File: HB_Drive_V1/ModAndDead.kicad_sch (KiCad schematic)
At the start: 24 parts, among them J501 Conn_01x02, J502 Conn_01x02, U501 74LS08, U502 74AUC2G02, U503 74LS365, U504 LM311

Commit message: updates board to highest working copy
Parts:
- removed C501, C502, C505, C506, C507, C508: 100nF 100V, Capacitor_SMD:C_0603_1608Metric, symbol Device:C
- removed C503, C504: 470pF 50V, Capacitor_SMD:C_0603_1608Metric, symbol Device:C
- removed J501, J502: Conn_01x02, Jumper:SolderJumper-2_P1.3mm_Open_TrianglePad1.0x1.5mm, symbol Connector_Generic:Conn_01x02
- removed R501, R502: PV36W502C01B00, POT_PV36W_BRN, symbol POT_PV36W_BRN:PV36W502C01B00
- removed R503, R504: 500Ω, Resistor_SMD:R_0603_1608Metric_Pad0.98x0.95mm_HandSolder, symbol Device:R_Small_US
- removed R505, R506: 100KΩ, Resistor_SMD:R_0603_1608Metric_Pad0.98x0.95mm_HandSolder, symbol Device:R_Small_US
- removed R507, R508, R509: 1KΩ, Resistor_SMD:R_0603_1608Metric_Pad0.98x0.95mm_HandSolder, symbol Device:R_Small_US
- removed TP501: TestPoint, TestPoint:TestPoint_Loop_D2.60mm_Drill1.6mm_Beaded, symbol Connector:TestPoint
- removed U501: 74LS08, symbol 74xx:74LS08
- removed U502: 74AUC2G02, symbol 74xGxx:74AUC2G02
- removed U503: 74LS365, symbol 74xx:74LS365
- removed U504: LM311, symbol Comparator:LM311
- added C401, C402, C403, C404, C405, C408: 100nF 100V, Capacitor_SMD:C_0603_1608Metric, symbol Device:C
- added C406, C407: 470pF 50V, Capacitor_SMD:C_0603_1608Metric, symbol Device:C
- added J401, J402: Conn_01x02, Jumper:SolderJumper-2_P1.3mm_Open_TrianglePad1.0x1.5mm, symbol Connector_Generic:Conn_01x02
- added R401, R402, R403: 1KΩ, Resistor_SMD:R_0603_1608Metric_Pad0.98x0.95mm_HandSolder, symbol Device:R_Small_US
- added R404, R405: PV36W502C01B00, POT_PV36W_BRN, symbol POT_PV36W_BRN:PV36W502C01B00
- added R406, R407: 500Ω, Resistor_SMD:R_0603_1608Metric_Pad0.98x0.95mm_HandSolder, symbol Device:R_Small_US
- added R408, R409: 100KΩ, Resistor_SMD:R_0603_1608Metric_Pad0.98x0.95mm_HandSolder, symbol Device:R_Small_US
- added TP401: TestPoint, TestPoint:TestPoint_Loop_D2.60mm_Drill1.6mm_Beaded, symbol Connector:TestPoint
- added U401: LM311, Package_SO:SOIC-8_3.9x4.9mm_P1.27mm, symbol Comparator:LM311
- added U402: 74LS08, Package_SO:SOIC-14_3.9x8.7mm_P1.27mm, symbol 74xx:74LS08
- added U403: 74AUC2G02, Package_SO:VSSOP-8_2.3x2mm_P0.5mm, symbol 74xGxx:74AUC2G02
- added U404: 74LS365, Package_SO:SOIC-16_3.9x9.9mm_P1.27mm, symbol 74xx:74LS365
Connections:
- net +15V: now also C401.1, U401.8 (V+)
- net +5V: now also C403.2, C404.2, C405.2, C408.2, R403.2, U402.7 (GND), U403.4 (GND), U404.16 (VCC)
- net -15V: now also C402.1, U401.4 (V-)
- net Carrier: now also R402.1
- net D_Cmd: now also R401.1
- net GND: now also C401.2, C402.2, C403.1, C404.1, C405.1, C406.2, C407.2, C408.1, R408.2, R409.2, U401.1 (GND), U402.14 (VCC), U403.8 (VCC), U404.1 (E1), U404.12 (I5), U404.14 (I6), U404.15 (E2), U404.4 (I2), U404.6 (I3), U404.8 (GND)
- net G_Lower_Cmd: now also U402.6
- net G_Upper_Cmd: now also U402.3
- net HS_Buf_In: now also C406.1, J401.2 (Pin_2), R406.2, R408.1, U404.2 (I1)
- net HS_Buf_Out: now also J401.1 (Pin_1), U402.2, U404.3 (O1)
- net H_Cmd: now also R403.1, R404.1, R404.2, TP401.1, U401.7, U402.1, U403.1, U403.2
- net LS_Buf_In: now also C407.1, J402.2 (Pin_2), R407.2, R409.1, U404.10 (I4)
- net LS_Buf_Out: now also J402.1 (Pin_1), U402.5, U404.9 (O4)
- new net: R405.3, R407.1
- new net: R401.2, U401.2 (+)
- new net: R404.3, R406.1
- new net: R402.2, U401.3 (-)
- new net: R405.1, R405.2, U402.4, U403.7

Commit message: updates board to REV 1 Ordered version
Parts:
- added unit 2 of U403
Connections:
- net GND: now also U403.5, U403.6
- no-connect marks 6 -> 7
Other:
- note added: "unused NOR 403B on 74AUC2G02 Dual Package"
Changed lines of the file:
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@@
 	)
 	(rectangle
-		(start 171.45 74.93)
+		(start 171.45 58.42)
 		(end 331.47 139.7)
 		(stroke
@@
 	)
 	(rectangle
+		(start 201.93 64.77)
+		(end 252.73 68.58)
+		(stroke
+			(width 0)
+			(type default)
+		)
+		(fill
+			(type none)
+		)
+	)
+	(rectangle
 		(start 238.76 147.32)
 		(end 300.99 208.28)
@@
 		)
 	)
+	(text "unused NOR 403B on 74AUC2G02 Dual Package"
+		(exclude_from_sim no)
+		(at 227.33 66.802 0)
+		(effects
+			(font
+				(size 1.27 1.27)
+			)
+		)
+	)
 	(text "DUTY COMMAND TO CARRIER WAVE COMPARATOR"
 		(exclude_from_sim no)
@@
 	)
 	(junction
+		(at 180.34 78.74)
+		(diameter 0)
+		(color 0 0 0 0)
+	)
+	(junction
 		(at 140.97 97.79)
 		(diameter 0)
@@
 	)
 	(no_connect
+		(at 208.28 76.2)
+	)
+	(no_connect
 		(at 280.67 180.34)
 	)
@@
 	(wire
 		(pts
+			(xy 180.34 73.66) (xy 180.34 78.74)
+		)
+		(stroke
+			(width 0)
+			(type default)
+		)
+	)
+	(wire
+		(pts
 			(xy 252.73 195.58) (xy 267.97 195.58)
 		)
@@
 	(wire
 		(pts
+			(xy 180.34 78.74) (xy 180.34 81.28)
+		)
+		(stroke
+			(width 0)
+			(type default)
+		)
+	)
+	(wire
+		(pts
 			(xy 107.95 113.03) (xy 107.95 107.95)
 		)
@@
 	)
 	(symbol
+		(lib_id "74xGxx:74AUC2G02")
+		(at 195.58 76.2 0)
+		(unit 2)
+		(body_style 1)
+		(exclude_from_sim no)
+		(in_bom yes)
+		(on_board yes)
+		(in_pos_files yes)
+		(dnp no)
+		(fields_autoplaced yes)
+		(property "Reference" "U403"
+			(at 194.31 66.04 0)
+			(show_name no)
+			(do_not_autoplace no)
+			(effects
+				(font
+					(size 1.27 1.27)
+				)
+			)
+		)
+		(property "Value" "74AUC2G02"
+			(at 194.31 68.58 0)
+			(show_name no)
+			(do_not_autoplace no)
+			(effects
+				(font
+					(size 1.27 1.27)
+				)
+			)
+		)
+		(property "Footprint" "Package_SO:VSSOP-8_2.3x2mm_P0.5mm"
+			(at 195.58 76.2 0)
+			(hide yes)
+			(show_name no)
+			(do_not_autoplace no)
+			(effects
+				(font
+					(size 1.27 1.27)
+				)
+			)
+		)
+		(property "Datasheet" "http://www.ti.com/lit/sg/scyt129e/scyt129e.pdf"
+			(at 195.58 76.2 0)
+			(hide yes)
+			(show_name no)
+			(do_not_autoplace no)
+			(effects
+				(font
+					(size 1.27 1.27)
+				)
+			)
+		)
+		(property "Description" "Dual NOR Gate, Low-Voltage CMOS"
+			(at 195.58 76.2 0)
+			(hide yes)
+			(show_name no)
+			(do_not_autoplace no)
+			(effects
+				(font
+					(size 1.27 1.27)
+				)
+			)
+		)
+		(pin "8"
+		)
+		(pin "3"
+		)
+		(pin "4"
+		)
+		(pin "6"
+		)
+		(pin "2"
+		)
+		(pin "5"
+		)
+		(pin "7"
+		)
+		(pin "1"
+		)
+		(instances
+			(project "HB_Drive_V1"
+				(path "/a9b54c89-4c8e-4c90-8a0d-ec2009e369b7/28e2d9d3-ebce-4623-8c7e-52f93025d826/97cfd595-263d-4fe9-9bac-f56dcdbd61fb"
+					(reference "U403")
+					(unit 2)
+				)
+			)
+		)
+	)
+	(symbol
 		(lib_id "Device:C")
 		(at 259.08 125.73 0)
@@
 					(unit 1)
 				)
+			)
+		)
+	)
+	(symbol
+		(lib_id "power:GND")
+		(at 180.34 81.28 0)
+		(unit 1)
+		(body_style 1)
+		(exclude_from_sim no)
+		(in_bom yes)
+		(on_board yes)
+		(in_pos_files yes)
+		(dnp no)
+		(property "Reference" "#PWR0419"
+			(at 180.34 87.63 0)
+			(hide yes)
+			(show_name no)
+			(do_not_autoplace no)
+			(effects
+				(font
+					(size 1.27 1.27)
+				)
+			)
+		)
+		(property "Value" "GND"
+			(at 183.896 84.582 0)
+			(show_name no)
+			(do_not_autoplace no)
+			(effects
+				(font
+					(size 1.27 1.27)
+				)
+			)
+		)
+		(property "Footprint" ""
+			(at 180.34 81.28 0)
+			(hide yes)
+			(show_name no)
+			(do_not_autoplace no)
+			(effects
+				(font
+					(size 1.27 1.27)
+				)
+			)
+		)
+		(property "Datasheet" ""
+			(at 180.34 81.28 0)
+			(hide yes)
+			(show_name no)
+			(do_not_autoplace no)
+			(effects
+				(font
+					(size 1.27 1.27)
+				)
+			)
+		)
+		(property "Description" "Power symbol creates a global label with name \"GND\" , ground"
+			(at 180.34 81.28 0)
+			(hide yes)
+			(show_name no)
+			(do_not_autoplace no)
+			(effects
+				(font
+					(size 1.27 1.27)
+				)
+			)
+		)
+		(pin "1"
+		)
+		(instances
+			(project "HB_Drive_V1"
+				(path "/a9b54c89-4c8e-4c90-8a0d-ec2009e369b7/28e2d9d3-ebce-4623-8c7e-52f93025d826/97cfd595-263d-4fe9-9bac-f56dcdbd61fb"
+					(reference "#PWR0419")
+					(unit 1)
+				)

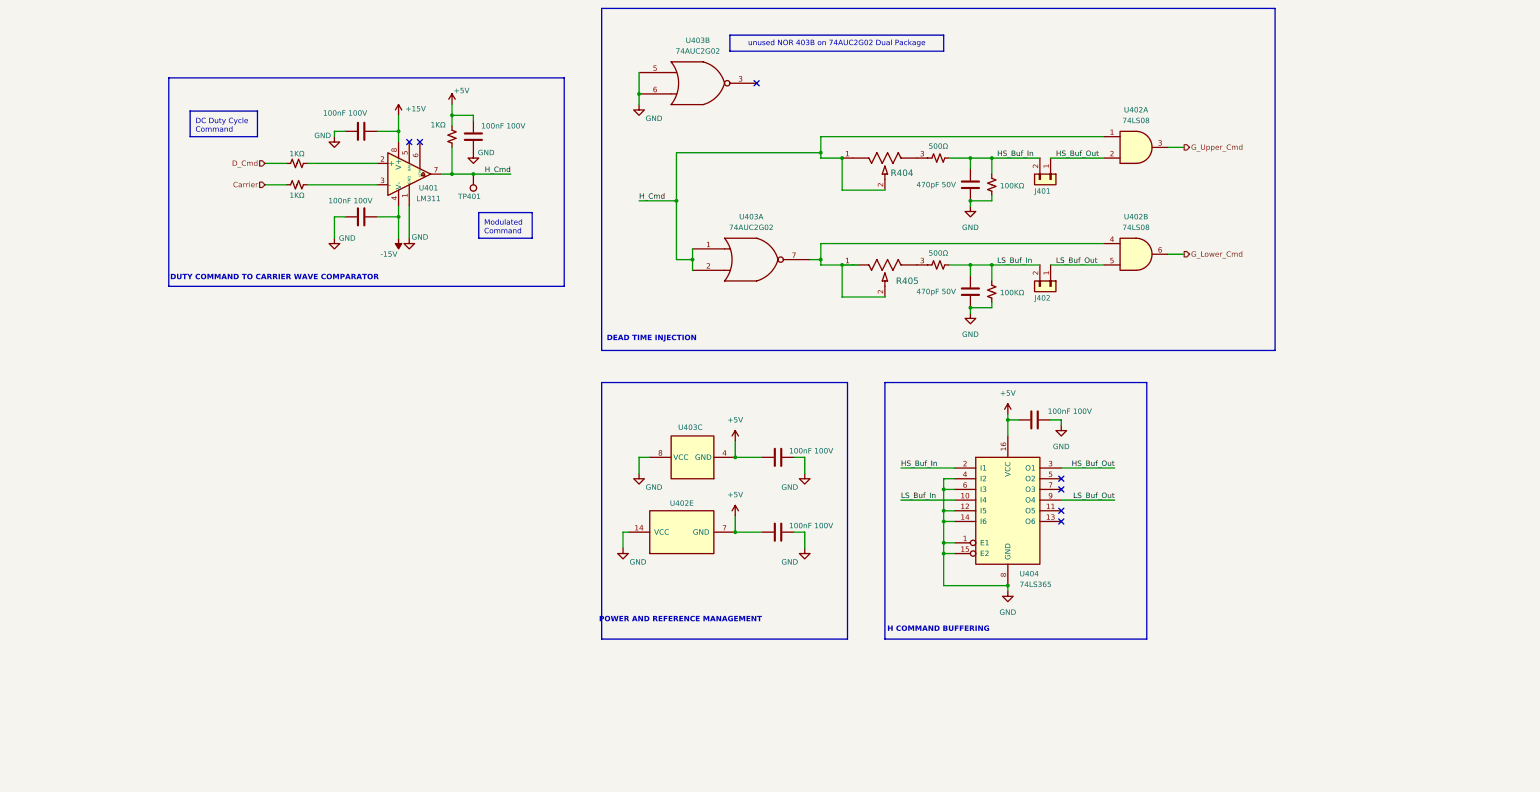
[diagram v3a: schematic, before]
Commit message: Annotates Schematic! Fixes REV1 wiring swaps and replaces buffer
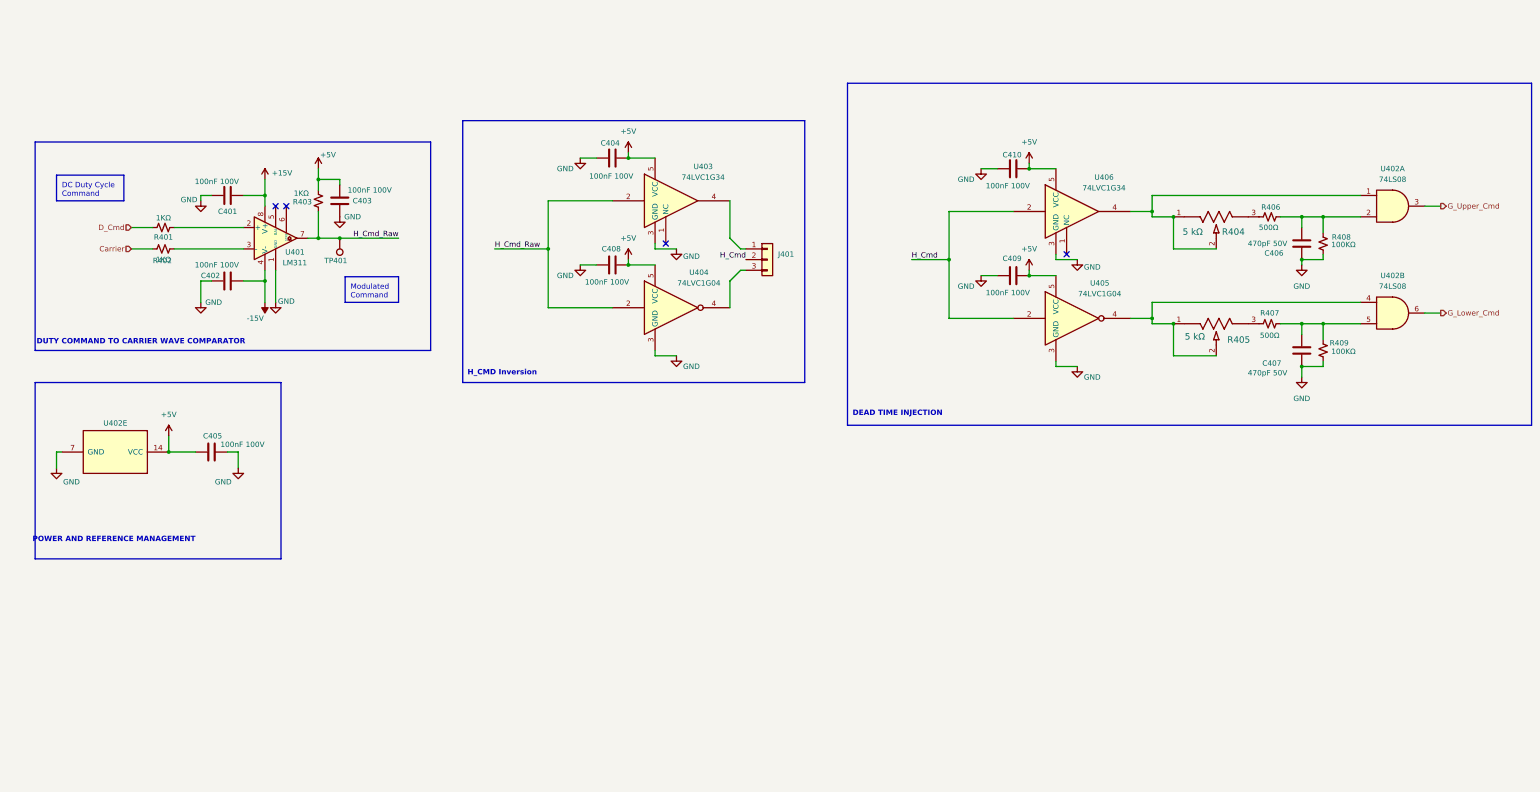
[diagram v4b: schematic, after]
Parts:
- removed J401, J402: Conn_01x02, Jumper:SolderJumper-2_P1.3mm_Open_TrianglePad1.0x1.5mm, symbol Connector_Generic:Conn_01x02
- removed U403: 74AUC2G02, Package_SO:VSSOP-8_2.3x2mm_P0.5mm, symbol 74xGxx:74AUC2G02
- removed U404: 74LS365, Package_SO:SOIC-16_3.9x9.9mm_P1.27mm, symbol 74xx:74LS365
- added C409, C410: 100nF 100V, Capacitor_SMD:C_0603_1608Metric, symbol Device:C
- added J401: Conn_01x03, symbol Connector_Generic:Conn_01x03
- added U403, U406: 74LVC1G34, symbol 74xGxx:74LVC1G34
- added U404, U405: 74LVC1G04, symbol 74xGxx:74LVC1G04
- R404, R405: value PV36W502C01B00 -> 5 kΩ; footprint POT_PV36W_BRN -> PV36W104C01B00:POT_PV36W_BRN
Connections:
- net HS_Buf_Out is gone; now on an unnamed net: U402.2
- net LS_Buf_Out is gone; now on an unnamed net: U402.5
- net +5V: now also C404.1, C408.1, U402.14 (VCC), C409.1, C410.1, U403.5 (VCC), U404.5 (VCC), U405.5 (VCC), U406.5 (VCC); no longer C404.2, C408.2, U402.7 (GND)
- net GND: now also C404.2, C408.2, U402.7 (GND), C409.2, C410.2, U403.3 (GND), U404.3 (GND), U405.3 (GND), U406.3 (GND); no longer C404.1, C408.1, U402.14 (VCC)
- net H_Cmd: now also J401.2 (Pin_2), U405.2, U406.2; no longer R403.1, R404.1, R404.2, TP401.1, U401.7, U402.1
- net at R405.1, R405.2, U402.4: now also U405.4
- net HS_Buf_In: no longer names the net of C406.1, R406.2, R408.1
- net LS_Buf_In: no longer names the net of C407.1, R407.2, R409.1
- new net: R404.1, R404.2, U402.1, U406.4
- new net: J401.1 (Pin_1), U403.4
- new net: J401.3 (Pin_3), U404.4
- new net H_Cmd_Raw: R403.1, TP401.1, U401.7, U403.2, U404.2
- no-connect marks 7 -> 4
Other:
- note added: "H_CMD Inversion"
- note removed: "H COMMAND BUFFERING"
- note removed: "unused NOR 403B on 74AUC2G02 Dual Package"
- moved on the sheet: R404, R405, TP401, U401, U402A, U402B

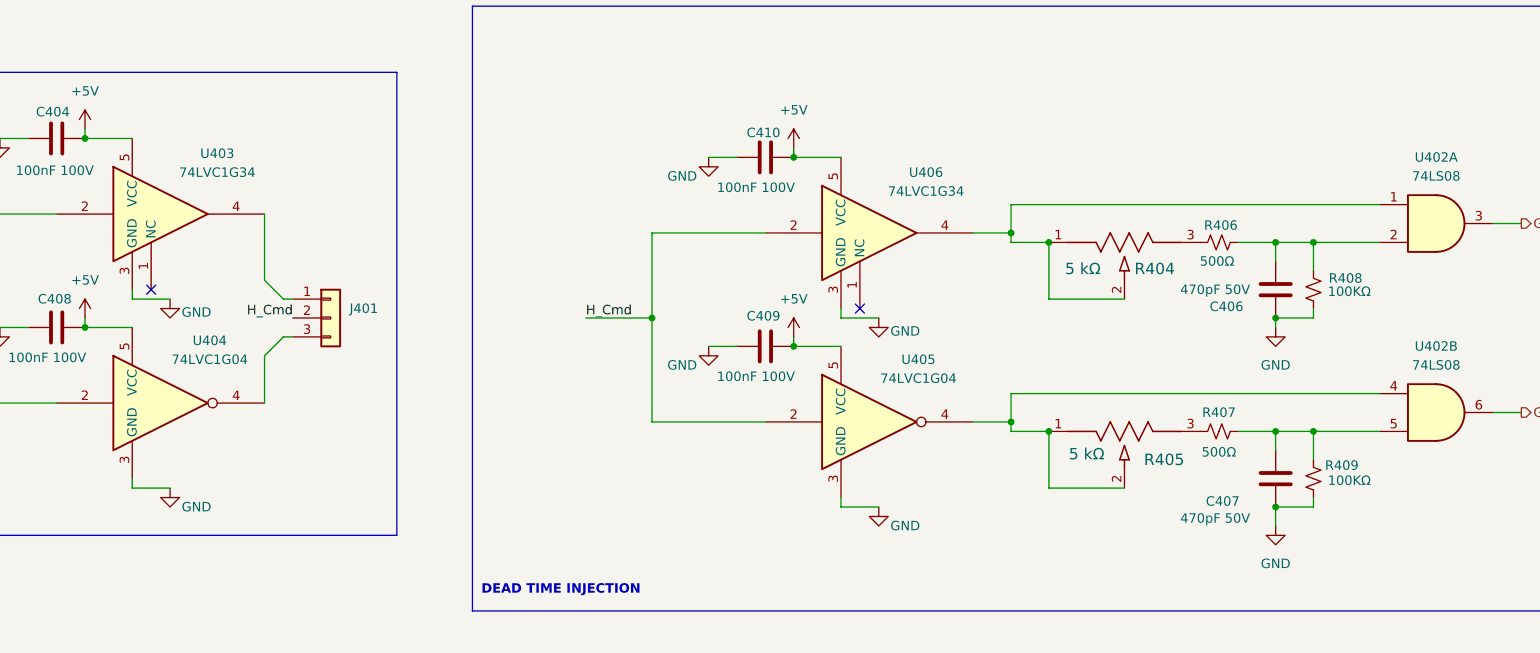
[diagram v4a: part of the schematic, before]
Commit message: annotates PCB! wiring is still broken here
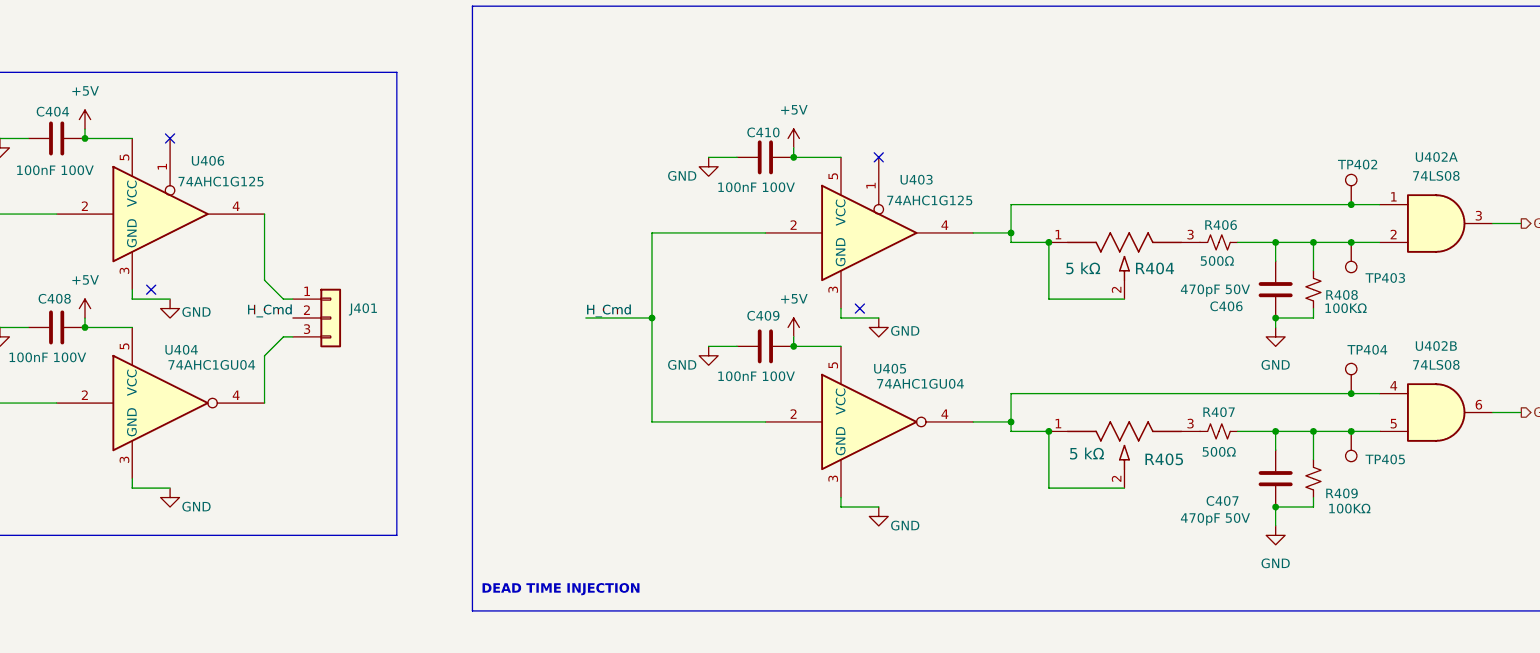
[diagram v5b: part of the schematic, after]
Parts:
- removed U403, U406: 74LVC1G34, symbol 74xGxx:74LVC1G34
- removed U404, U405: 74LVC1G04, symbol 74xGxx:74LVC1G04
- added TP402, TP403, TP404, TP405: TestPoint, TestPoint:TestPoint_Loop_D2.60mm_Drill1.6mm_Beaded, symbol Connector:TestPoint
- added U403, U406: 74AHC1G125, Package_TO_SOT_SMD:SOT-23-5, symbol 74xGxx:74AHC1G125
- added U404, U405: 74AHC1GU04, Package_TO_SOT_SMD:SOT-23-5, symbol 74xGxx:74AHC1GU04
- J401: footprint (none) -> Connector_PinHeader_2.54mm:PinHeader_1x03_P2.54mm_Vertical
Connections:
- net +5V: now also U403.5 (VCC), U404.5 (VCC), U405.5 (VCC), U406.5 (VCC)
- net GND: now also U403.3 (GND), U404.3 (GND), U405.3 (GND), U406.3 (GND)
- net H_Cmd: now also U403.2, U405.2
- net H_Cmd_Raw: now also U404.2, U406.2
- net at C407.1, R407.2, R409.1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: now also TP405.1
- net at R404.1, R404.2, U402.1: now also TP402.1, U403.4
- net at C406.1, R406.2, R408.1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: now also TP403.1
- net at J401.1 (Pin_1): now also U406.4
- net at R405.1, R405.2, U402.4: now also TP404.1, U405.4
- net at J401.3 (Pin_3): now also U404.4
- no-connect marks 4 -> 6
